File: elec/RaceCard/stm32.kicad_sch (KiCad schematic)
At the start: 10 parts, among them J1 Conn_ST_STDC14, U1 STM32U031C6Tx

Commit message: Commence plugger choses
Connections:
- no-connect marks 0 -> 41
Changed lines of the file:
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@@
 		(color 0 0 0 0)
 	)
+	(no_connect
+		(at 154.94 30.48)
+	)
+	(no_connect
+		(at 205.74 60.96)
+	)
+	(no_connect
+		(at 167.64 30.48)
+	)
+	(no_connect
+		(at 162.56 60.96)
+	)
+	(no_connect
+		(at 137.16 50.8)
+	)
+	(no_connect
+		(at 175.26 30.48)
+	)
+	(no_connect
+		(at 203.2 60.96)
+	)
+	(no_connect
+		(at 182.88 60.96)
+	)
+	(no_connect
+		(at 170.18 60.96)
+	)
+	(no_connect
+		(at 144.78 60.96)
+	)
+	(no_connect
+		(at 167.64 60.96)
+	)
+	(no_connect
+		(at 185.42 60.96)
+	)
+	(no_connect
+		(at 200.66 60.96)
+	)
+	(no_connect
+		(at 177.8 60.96)
+	)
+	(no_connect
+		(at 195.58 60.96)
+	)
+	(no_connect
+		(at 266.7 40.64)
+	)
+	(no_connect
+		(at 175.26 60.96)
+	)
+	(no_connect
+		(at 198.12 60.96)
+	)
+	(no_connect
+		(at 182.88 30.48)
+	)
+	(no_connect
+		(at 165.1 30.48)
+	)
+	(no_connect
+		(at 266.7 43.18)
+	)
+	(no_connect
+		(at 152.4 60.96)
+	)
+	(no_connect
+		(at 147.32 30.48)
+	)
+	(no_connect
+		(at 162.56 30.48)
+	)
+	(no_connect
+		(at 187.96 60.96)
+	)
+	(no_connect
+		(at 152.4 30.48)
+	)
+	(no_connect
+		(at 266.7 48.26)
+	)
+	(no_connect
+		(at 180.34 60.96)
+	)
+	(no_connect
+		(at 266.7 53.34)
+	)
+	(no_connect
+		(at 157.48 60.96)
+	)
+	(no_connect
+		(at 172.72 60.96)
+	)
+	(no_connect
+		(at 193.04 60.96)
+	)
+	(no_connect
+		(at 160.02 30.48)
+	)
+	(no_connect
+		(at 149.86 30.48)
+	)
+	(no_connect
+		(at 144.78 30.48)
+	)
+	(no_connect
+		(at 147.32 60.96)
+	)
+	(no_connect
+		(at 160.02 60.96)
+	)
+	(no_connect
+		(at 170.18 30.48)
+	)
+	(no_connect
+		(at 190.5 60.96)
+	)
+	(no_connect
+		(at 157.48 30.48)
+	)
+	(no_connect
+		(at 266.7 55.88)
+	)
 	(wire
 		(pts
@@
 	(wire
 		(pts
+			(xy 19.05 21.59) (xy 20.32 21.59)
+		)
+		(stroke
+			(width 0)
+			(type default)
+		)
+	)
+	(wire
+		(pts
 			(xy 251.46 60.96) (xy 251.46 64.77)
 		)
@@
 	(wire
 		(pts
-			(xy 20.32 22.86) (xy 20.32 27.94)
-		)
-		(stroke
-			(width 0)
-			(type default)
-		)
-	)
-	(wire
-		(pts
 			(xy 266.7 35.56) (xy 270.51 35.56)
 		)
@@
 		(pts
 			(xy 213.36 45.72) (xy 215.9 45.72)
+		)
+		(stroke
+			(width 0)
+			(type default)
+		)
+	)
+	(wire
+		(pts
+			(xy 20.32 21.59) (xy 20.32 27.94)
 		)
 		(stroke
@@
 				(hide yes)
 			)
+		)
+	)
+	(hierarchical_label "VDD"
+		(shape input)
+		(at 19.05 21.59 180)
+		(effects
+			(font
+				(size 1.27 1.27)
+			)
+			(justify right)
 		)
 	)
@@
 	)
 	(symbol
-		(lib_id "power:VDD")
-		(at 20.32 25.4 0)
-		(unit 1)
-		(exclude_from_sim no)
-		(in_bom yes)
-		(on_board yes)
-		(dnp no)
-		(fields_autoplaced yes)
-		(property "Reference" "#PWR01"
-			(at 20.32 29.21 0)
-			(effects
-				(font
-					(size 1.27 1.27)
-				)
-				(hide yes)
-			)
-		)
-		(property "Value" "VDD"
-			(at 20.32 20.32 0)
-			(effects
-				(font
-					(size 1.27 1.27)
-				)
-			)
-		)
-		(property "Footprint" ""
-			(at 20.32 25.4 0)
-			(effects
-				(font
-					(size 1.27 1.27)
-				)
-				(hide yes)
-			)
-		)
-		(property "Datasheet" ""
-			(at 20.32 25.4 0)
-			(effects
-				(font
-					(size 1.27 1.27)
-				)
-				(hide yes)
-			)
-		)
-		(property "Description" "Power symbol creates a global label with name \"VDD\""
-			(at 20.32 25.4 0)
-			(effects
-				(font
-					(size 1.27 1.27)
-				)
-				(hide yes)
-			)
-		)
-		(pin "1"
-		)
-		(instances
-			(project "RaceCard"
-				(path "/fef6ab1d-cc84-41bb-aff7-8da28fd37bf7/4fa2e0fb-f6ed-42f5-9bb3-15e1a8421f43"
-					(reference "#PWR01")
-					(unit 1)
-				)
-			)
-		)
-	)
-	(symbol
 		(lib_id "power:GND")
 		(at 222.25 48.26 0)
@@
 		(on_board yes)
 		(dnp no)
-		(fields_autoplaced yes)
 		(property "Reference" "U1"
 			(at 213.36 41.0367 0)
@@
 	(symbol
 		(lib_id "power:VDD")
-		(at 116.84 40.64 90)
+		(at 114.3 43.18 0)
 		(unit 1)
 		(exclude_from_sim no)
@@
 		(dnp no)
 		(property "Reference" "#PWR07"
-			(at 120.65 40.64 0)
+			(at 114.3 46.99 0)
 			(effects
 				(font
@@
 		)
 		(property "Value" "VDD"
-			(at 110.49 40.64 90)
+			(at 114.3 36.83 0)
 			(effects
 				(font
@@
 		)
 		(property "Footprint" ""
-			(at 116.84 40.64 0)
+			(at 114.3 43.18 0)
 			(effects
 				(font
@@
 		)
 		(property "Datasheet" ""
-			(at 116.84 40.64 0)
+			(at 114.3 43.18 0)
 			(effects
 				(font
@@
 		)
 		(property "Description" "Power symbol creates a global label with name \"VDD\""
-			(at 116.84 40.64 0)
-			(effects
-				(font
+			(at 114.3 43.18 0)
+			(effects
+				(font

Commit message: ajout connecteur usb c et leds
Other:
- moved on the sheet: C2, C3, C4, C5, C6, C7

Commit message: + connections stm et autres
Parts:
- J1: footprint C3I:CONN_3020-14-0300-00_CNC -> C3I_A25:CONN_3020-14-0300-00_CNC
- R1: value R0 -> 0
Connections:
- net AGND is gone; now on net GND: C6.2, C7.2, U1.8 (VSSA)
- net PA1/DATA: now reaches U1.11 (PA1)
- net PA6/MCLR: now reaches U1.16 (PA6)
- net PA7/RDY: now reaches U1.17 (PA7)
- net PB8/I2C1_SCL: now reaches U1.45 (PB8)
- net PB9/I2C1_SDA: now reaches U1.46 (PB9)
- no-connect marks 41 -> 37
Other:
- moved on the sheet: R1, U1

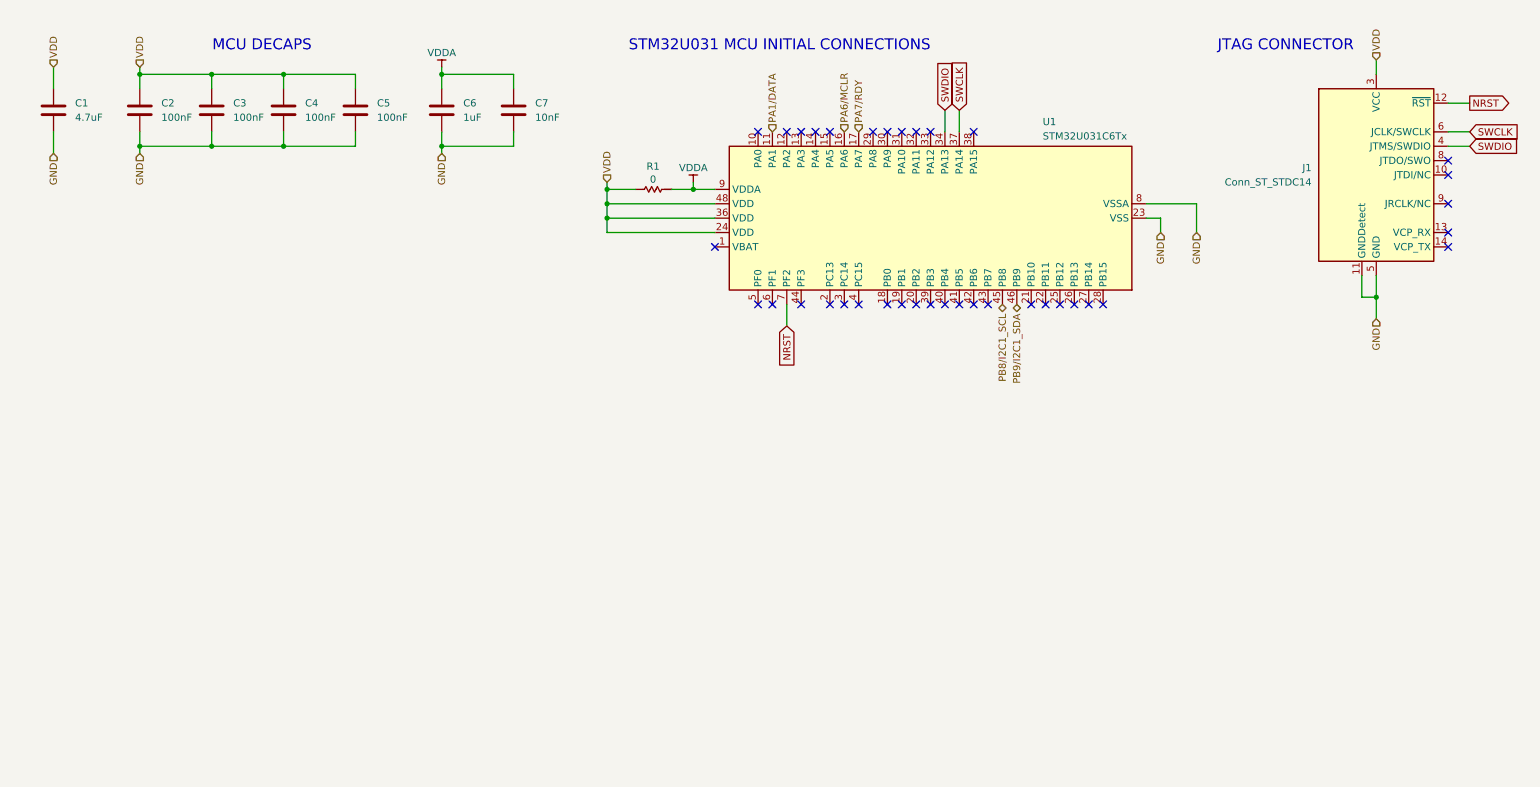
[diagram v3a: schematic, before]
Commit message: + test points
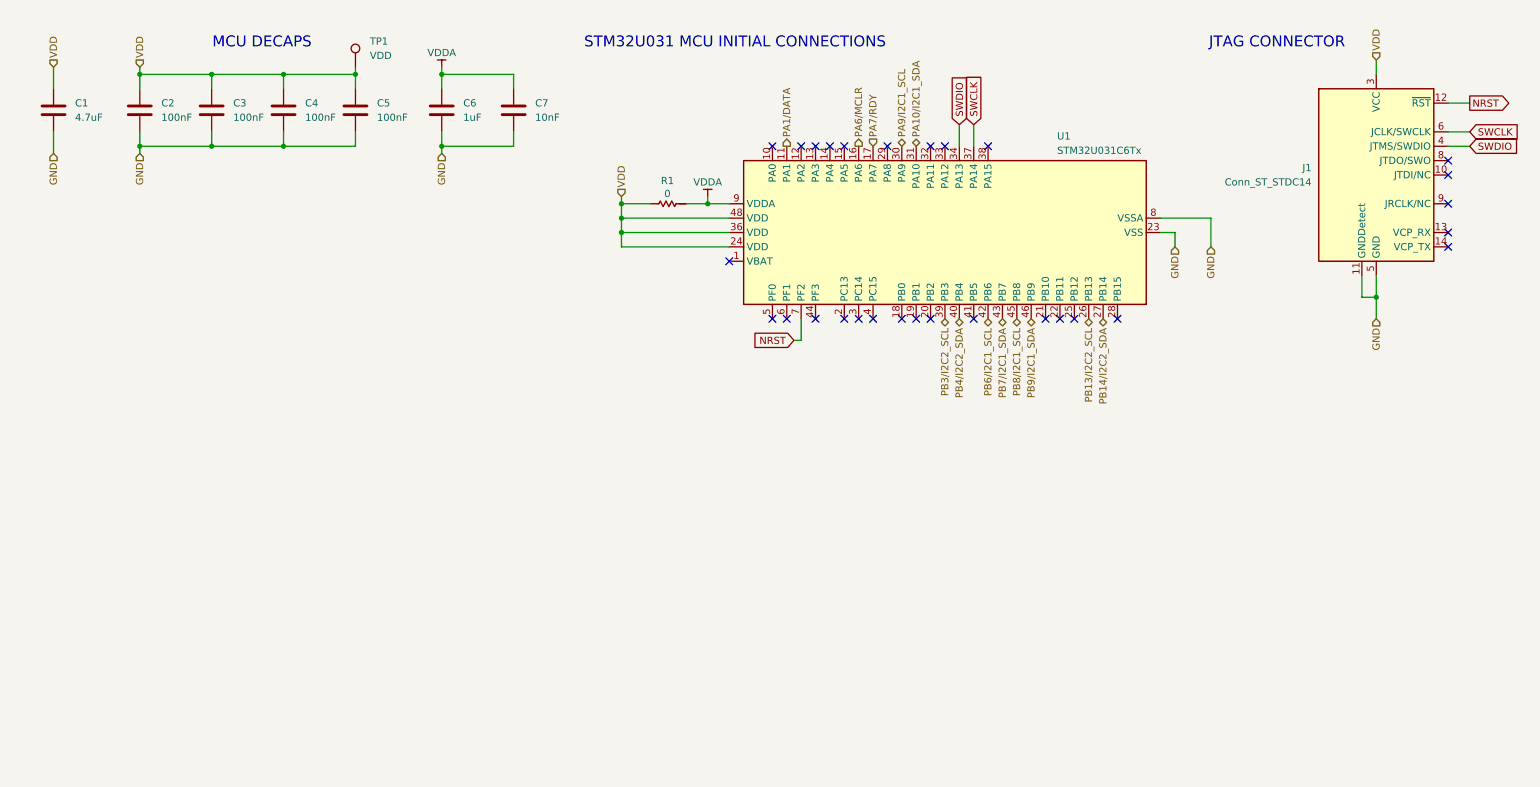
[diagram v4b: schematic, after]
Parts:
- added TP1: VDD, TestPoint:TestPoint_THTPad_3.0x3.0mm_Drill1.5mm, symbol Connector:TestPoint
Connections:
- net VDD: now also TP1.1
- net PB13/I2C2_SCL: now reaches U1.26 (PB13)
- net PB14/I2C2_SDA: now reaches U1.27 (PB14)
- net PA9/I2C1_SCL: now reaches U1.30 (PA9)
- net PA10/I2C1_SDA: now reaches U1.31 (PA10)
- net PB3/I2C2_SCL: now reaches U1.39 (PB3)
- net PB4/I2C2_SDA: now reaches U1.40 (PB4)
- net PB6/I2C1_SCL: now reaches U1.42 (PB6)
- net PB7/I2C1_SDA: now reaches U1.43 (PB7)
- no-connect marks 37 -> 29
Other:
- moved on the sheet: R1, U1

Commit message: + BOM
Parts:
- C1, C2, C3, C4, C5, C6, C7: footprint (none) -> Capacitor_SMD:C_0603_1608Metric
- R1: footprint (none) -> Resistor_SMD:R_0603_1608Metric
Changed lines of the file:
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@@
 			)
 		)
-		(property "Footprint" ""
+		(property "Footprint" "Capacitor_SMD:C_0603_1608Metric"
 			(at 36.5252 35.56 0)
 			(effects
@@
 			)
 		)
-		(property "Footprint" ""
+		(property "Footprint" "Resistor_SMD:R_0603_1608Metric"
 			(at 129.794 47.244 90)
 			(effects
@@
 			)
 		)
-		(property "Footprint" ""
+		(property "Footprint" "Capacitor_SMD:C_0603_1608Metric"
 			(at 102.5652 35.56 0)
 			(effects
@@
 			)
 		)
-		(property "Footprint" ""
+		(property "Footprint" "Capacitor_SMD:C_0603_1608Metric"
 			(at 89.8652 35.56 0)
 			(effects
@@
 			)
 		)
-		(property "Footprint" ""
+		(property "Footprint" "Capacitor_SMD:C_0603_1608Metric"
 			(at 21.2852 35.56 0)
 			(effects
@@
 			)
 		)
-		(property "Footprint" ""
+		(property "Footprint" "Capacitor_SMD:C_0603_1608Metric"
 			(at 49.2252 35.56 0)
 			(effects
@@
 			)
 		)
-		(property "Footprint" ""
+		(property "Footprint" "Capacitor_SMD:C_0603_1608Metric"
 			(at 61.9252 35.56 0)
 			(effects
@@
 			)
 		)
-		(property "Footprint" ""
+		(property "Footprint" "Capacitor_SMD:C_0603_1608Metric"
 			(at 74.6252 35.56 0)
 			(effects

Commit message: Fix des footprints et edge cuts
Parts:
- renumbered TP1 to TP9
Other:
- note added: "VALIDER"
- moved on the sheet: R1
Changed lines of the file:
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@@
 		(rev "Rev.1")
 	)
+	(rectangle
+		(start 85.725 17.145)
+		(end 111.125 45.72)
+		(stroke
+			(width 0.254)
+			(type solid)
+			(color 255 0 0 1)
+		)
+		(fill
+			(type none)
+		)
+	)
 	(text "MCU DECAPS\n"
 		(exclude_from_sim no)
@@
 		)
 	)
+	(text "VALIDER"
+		(exclude_from_sim no)
+		(at 98.552 44.45 0)
+		(effects
+			(font
+				(size 1.27 1.27)
+				(thickness 0.254)
+				(bold yes)
+				(color 255 0 0 1)
+			)
+		)
+	)
 	(text "STM32U031 MCU INITIAL CONNECTIONS\n"
 		(exclude_from_sim no)
@@
 	(wire
 		(pts
-			(xy 120.65 48.26) (xy 125.73 48.26)
+			(xy 120.65 48.26) (xy 124.46 48.26)
 		)
 		(stroke
@@
 	(symbol
 		(lib_id "Device:R_US")
-		(at 129.54 48.26 90)
+		(at 128.27 48.26 90)
 		(unit 1)
 		(exclude_from_sim no)
@@
 		(dnp no)
 		(property "Reference" "R1"
-			(at 128.778 44.196 90)
+			(at 128.27 43.942 90)
 			(effects
 				(font
@@
 		)
 		(property "Value" "0"
-			(at 128.778 46.482 90)
+			(at 128.27 45.974 90)
 			(effects
 				(font
@@
 		)
 		(property "Footprint" "Resistor_SMD:R_0603_1608Metric"
-			(at 129.794 47.244 90)
+			(at 128.524 47.244 90)
 			(effects
 				(font
@@
 		)
 		(property "Datasheet" "~"
-			(at 129.54 48.26 0)
+			(at 128.27 48.26 0)
 			(effects
 				(font
@@
 		)
 		(property "Description" "Resistor, US symbol"
-			(at 129.54 48.26 0)
+			(at 128.27 48.26 0)
 			(effects
 				(font
@@
 		(dnp no)
 		(fields_autoplaced yes)
-		(property "Reference" "TP1"
+		(property "Reference" "TP9"
 			(at 76.2 19.5579 0)
 			(effects
@@
 			(project ""
 				(path "/fef6ab1d-cc84-41bb-aff7-8da28fd37bf7/4fa2e0fb-f6ed-42f5-9bb3-15e1a8421f43"
-					(reference "TP1")
+					(reference "TP9")
 					(unit 1)
 				)
@@
 	(symbol
 		(lib_id "power:VDD")
-		(at 135.89 49.53 0)
+		(at 135.89 46.99 0)
 		(unit 1)
 		(exclude_from_sim no)
@@
 		(dnp no)
 		(property "Reference" "#PWR06"
-			(at 135.89 53.34 0)
+			(at 135.89 50.8 0)
 			(effects
 				(font
@@
 		)
 		(property "Value" "VDDA"
-			(at 135.89 44.45 0)
+			(at 135.89 41.91 0)
 			(effects
 				(font
@@
 		)
 		(property "Footprint" ""
-			(at 135.89 49.53 0)
+			(at 135.89 46.99 0)
 			(effects
 				(font
@@
 		)
 		(property "Datasheet" ""
-			(at 135.89 49.53 0)
+			(at 135.89 46.99 0)
 			(effects
 				(font
@@
 		)
 		(property "Description" "Power symbol creates a global label with name \"VDD\""
-			(at 135.89 49.53 0)
+			(at 135.89 46.99 0)
 			(effects
 				(font
@@
 	(symbol
 		(lib_id "power:VDD")
-		(at 88.9 26.67 0)
+		(at 88.9 24.13 0)
 		(unit 1)
 		(exclude_from_sim no)
@@
 		(dnp no)
 		(property "Reference" "#PWR05"
-			(at 88.9 30.48 0)
+			(at 88.9 27.94 0)
 			(effects
 				(font
@@
 		)
 		(property "Value" "VDDA"
-			(at 88.9 21.59 0)
+			(at 88.9 19.05 0)
 			(effects
 				(font
@@
 		)
 		(property "Footprint" ""
-			(at 88.9 26.67 0)
+			(at 88.9 24.13 0)
 			(effects
 				(font
@@
 		)
 		(property "Datasheet" ""
-			(at 88.9 26.67 0)
+			(at 88.9 24.13 0)
 			(effects
 				(font
@@
 		)
 		(property "Description" "Power symbol creates a global label with name \"VDD\""
-			(at 88.9 26.67 0)
+			(at 88.9 24.13 0)
 			(effects
 				(font
@@
 			)
 		)
-		(property "Datasheet" "https://www.cnctech.us/pdfs/3020-XX-0300-00%20(9T).pdf"
+		(property "Datasheet" "https://www.st.com/content/ccc/resource/technical/document/user_manual/group1/99/49/91/b6/b2/3a/46/e5/DM00526767/files/DM00526767.pdf/jcr:content/translations/en.DM00526767.pdf"
 			(at 245.11 74.93 90)
 			(effects

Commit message: Power net update et cleanup sch
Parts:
- removed R1: 0, Resistor_SMD:R_0603_1608Metric, symbol Device:R_US
- added C6: 1uF, Capacitor_SMD:C_0603_1608Metric, symbol Device:C
- added C9: 100nF, Capacitor_SMD:C_0603_1608Metric, symbol Device:C
- added FB1: 120R, Inductor_SMD:L_0603_1608Metric, symbol Device:FerriteBead_Small
- added TP10: VDDA, TestPoint:TestPoint_THTPad_3.0x3.0mm_Drill1.5mm, symbol Connector:TestPoint
- renumbered C6 to C7, C7 to C8
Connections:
- net VDD is gone; now on net +3V3: C1.1, C2.1, C3.1, C4.1, C5.1, J1.3 (VCC), TP9.1, U1.24 (VDD), U1.36 (VDD), U1.48 (VDD)
- net GND: now also C6.2, C9.1
- net NRST: now also C9.2
- net +3V3: now reaches U1.1 (VBAT)
- net +3V3: now also C6.1, FB1.1
- net VDDA renamed +3V3A
- net +3V3A: now also FB1.2, TP10.1
- no-connect marks 29 -> 28
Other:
- note removed: "VALIDER"
- moved on the sheet: C7, C8

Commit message: Cleanup
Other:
- note removed: "JTAG CONNECTOR"
- note removed: "MCU DECAPS"
- note removed: "STM32U031 MCU INITIAL CONNECTIONS"
- moved on the sheet: C1, C2, C3, C4, C5, C6, C7, C8, C9, FB1, J1, TP10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
